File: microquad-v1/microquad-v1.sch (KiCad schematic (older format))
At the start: 22 parts

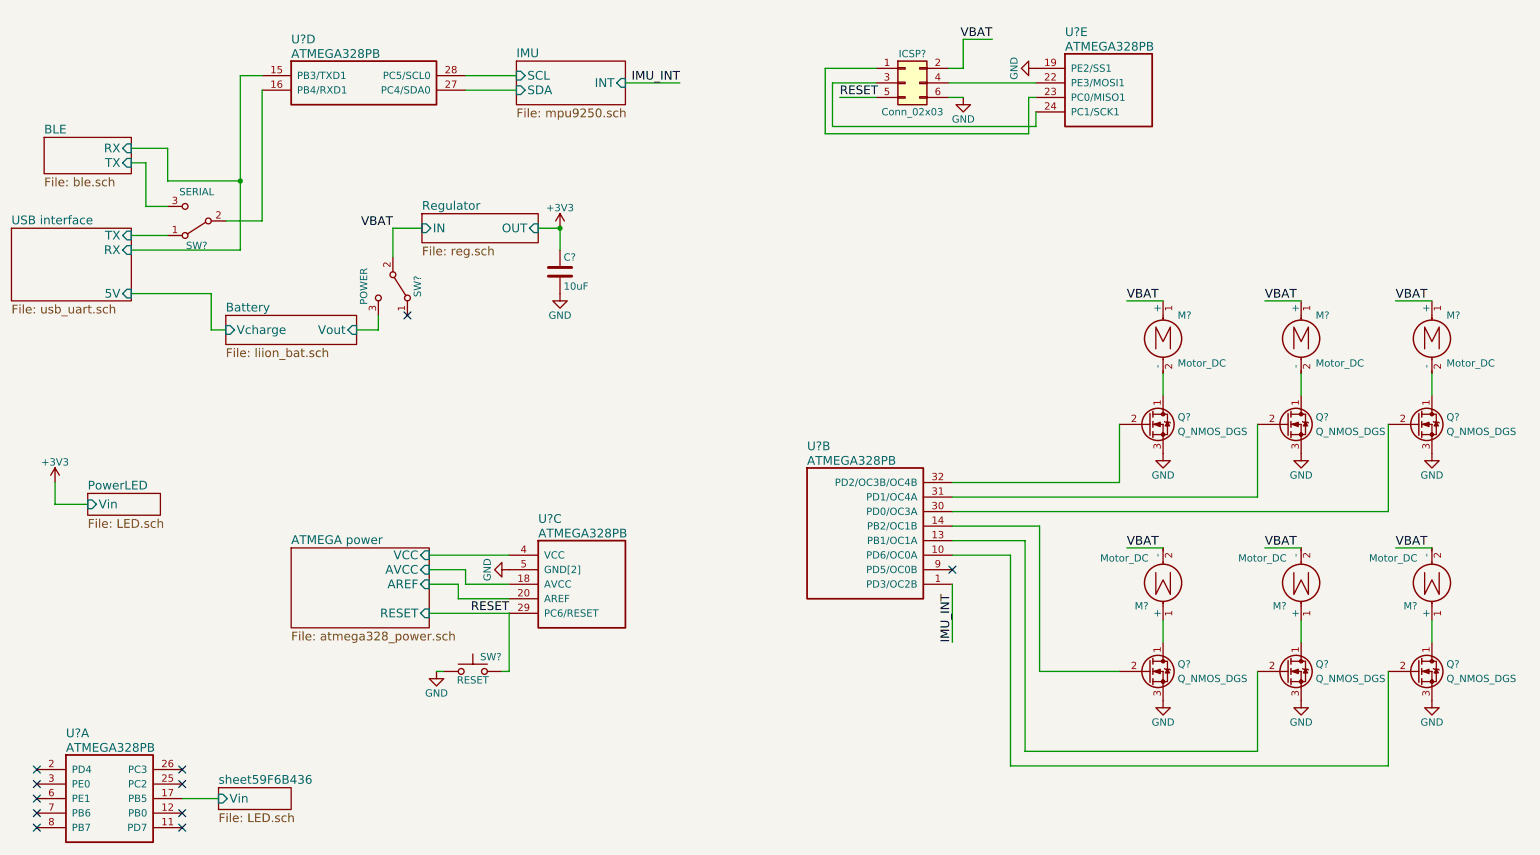
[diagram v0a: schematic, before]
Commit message: Fixed DRC errors (the ladybug is now happy)
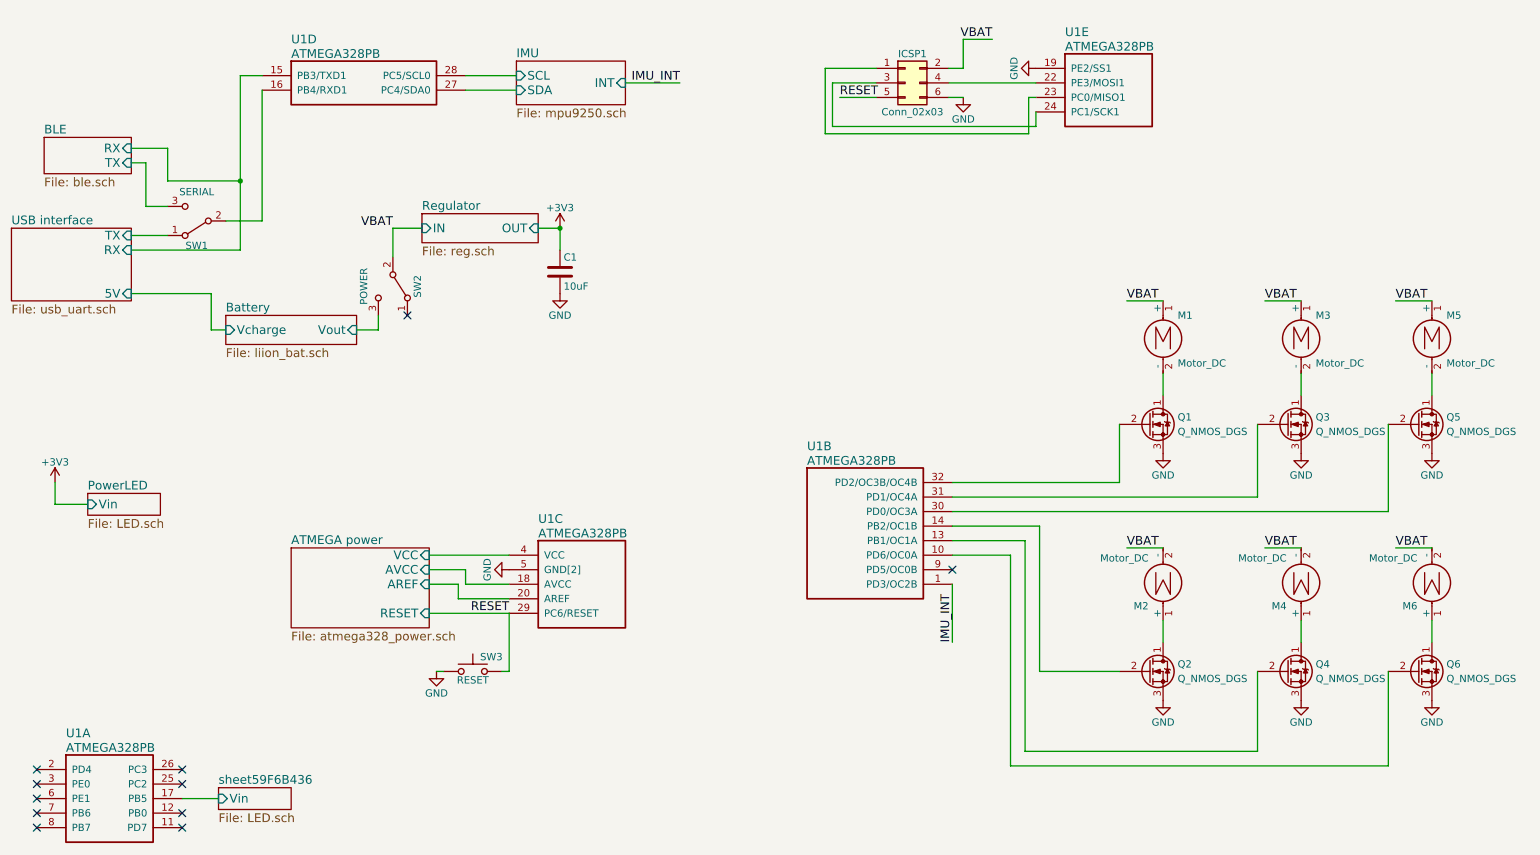
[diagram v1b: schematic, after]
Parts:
- gave numbers to parts that had none: 18
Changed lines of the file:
@@
 $Descr A4 11693 8268
 encoding utf-8
-Sheet 1 8
+Sheet 1 9
 Title ""
 Date ""
@@
 $EndSheet
 $Comp
-L ATMEGA328PB U?
+L ATMEGA328PB U1
 U 2 1 59F26F3B
 P 6000 4050
-F 0 "U?" H 6200 4300 60  0000 L CNN
+F 0 "U1" H 6200 4300 60  0000 L CNN
 F 1 "ATMEGA328PB" H 6200 4200 60  0000 L CNN
 F 2 "" H 6000 4050 60  0001 C CNN
@@
 $EndComp
 $Comp
-L ATMEGA328PB U?
+L ATMEGA328PB U1
 U 1 1 59F2742E
 P 900 6025
-F 0 "U?" H 1100 6275 60  0000 L CNN
+F 0 "U1" H 1100 6275 60  0000 L CNN
 F 1 "ATMEGA328PB" H 1100 6175 60  0000 L CNN
 F 2 "" H 900 6025 60  0001 C CNN
@@
 $EndComp
 $Comp
-L ATMEGA328PB U?
+L ATMEGA328PB U1
 U 3 1 59F274A5
 P 4150 4550
-F 0 "U?" H 4350 4800 60  0000 L CNN
+F 0 "U1" H 4350 4800 60  0000 L CNN
 F 1 "ATMEGA328PB" H 4350 4700 60  0000 L CNN
 F 2 "" H 4150 4550 60  0001 C CNN
@@
 $EndComp
 $Comp
-L ATMEGA328PB U?
+L ATMEGA328PB U1
 U 4 1 59F27516
 P 2450 1250
-F 0 "U?" H 2650 1500 60  0000 L CNN
+F 0 "U1" H 2650 1500 60  0000 L CNN
 F 1 "ATMEGA328PB" H 2650 1400 60  0000 L CNN
 F 2 "" H 2450 1250 60  0001 C CNN
@@
 $EndComp
 $Comp
-L ATMEGA328PB U?
+L ATMEGA328PB U1
 U 5 1 59F275A9
 P 7775 1200
-F 0 "U?" H 7975 1450 60  0000 L CNN
+F 0 "U1" H 7975 1450 60  0000 L CNN
 F 1 "ATMEGA328PB" H 7975 1350 60  0000 L CNN
 F 2 "" H 7775 1200 60  0001 C CNN
@@
 $EndComp
 $Comp
-L C C?
+L C C1
 U 1 1 59F54C39
 P 4500 2600
-F 0 "C?" H 4525 2700 50  0000 L CNN
+F 0 "C1" H 4525 2700 50  0000 L CNN
 F 1 "10uF" H 4525 2500 50  0000 L CNN
 F 2 "Capacitors_SMD:C_0805" H 4538 2450 50  0001 C CNN
@@
 NoConn ~ 3450 2900
 $Comp
-L Q_NMOS_DGS Q?
+L Q_NMOS_DGS Q1
 U 1 1 59F6C2EB
 P 8550 3650
-F 0 "Q?" H 8750 3700 50  0000 L CNN
+F 0 "Q1" H 8750 3700 50  0000 L CNN
 F 1 "Q_NMOS_DGS" H 8750 3600 50  0000 L CNN
 F 2 "" H 8750 3750 50  0001 C CNN
@@
 $EndComp
 $Comp
-L GND #PWR?
+L GND #PWR04
 U 1 1 59F6C628
 P 8650 3850
-F 0 "#PWR?" H 8650 3600 50  0001 C CNN
+F 0 "#PWR04" H 8650 3600 50  0001 C CNN
 F 1 "GND" H 8650 3700 50  0000 C CNN
 F 2 "" H 8650 3850 50  0001 C CNN
@@
 VBAT
 $Comp
-L Motor_DC M?
+L Motor_DC M1
 U 1 1 59F6E11F
 P 8650 3000
-F 0 "M?" H 8750 3100 50  0000 L CNN
+F 0 "M1" H 8750 3100 50  0000 L CNN
 F 1 "Motor_DC" H 8750 2800 50  0000 L TNN
 F 2 "" H 8650 2910 50  0001 C CNN
@@
 	8650 3300 8650 3450
 $Comp
-L Q_NMOS_DGS Q?
+L Q_NMOS_DGS Q3
 U 1 1 59F6F67A
 P 9500 3650
-F 0 "Q?" H 9700 3700 50  0000 L CNN
+F 0 "Q3" H 9700 3700 50  0000 L CNN
 F 1 "Q_NMOS_DGS" H 9700 3600 50  0000 L CNN
 F 2 "" H 9700 3750 50  0001 C CNN
@@
 $EndComp
 $Comp
-L GND #PWR?
+L GND #PWR05
 U 1 1 59F6F680
 P 9600 3850
-F 0 "#PWR?" H 9600 3600 50  0001 C CNN
+F 0 "#PWR05" H 9600 3600 50  0001 C CNN
 F 1 "GND" H 9600 3700 50  0000 C CNN
 F 2 "" H 9600 3850 50  0001 C CNN
@@
 VBAT
 $Comp
-L Motor_DC M?
+L Motor_DC M3
 U 1 1 59F6F688
 P 9600 3000
-F 0 "M?" H 9700 3100 50  0000 L CNN
+F 0 "M3" H 9700 3100 50  0000 L CNN
 F 1 "Motor_DC" H 9700 2800 50  0000 L TNN
 F 2 "" H 9600 2910 50  0001 C CNN
@@
 	9600 3300 9600 3450
 $Comp
-L Q_NMOS_DGS Q?
+L Q_NMOS_DGS Q5
 U 1 1 59F6F948
 P 10400 3650
-F 0 "Q?" H 10600 3700 50  0000 L CNN
+F 0 "Q5" H 10600 3700 50  0000 L CNN
 F 1 "Q_NMOS_DGS" H 10600 3600 50  0000 L CNN
 F 2 "" H 10600 3750 50  0001 C CNN
@@
 $EndComp
 $Comp
-L GND #PWR?
+L GND #PWR06
 U 1 1 59F6F94E
 P 10500 3850
-F 0 "#PWR?" H 10500 3600 50  0001 C CNN
+F 0 "#PWR06" H 10500 3600 50  0001 C CNN
 F 1 "GND" H 10500 3700 50  0000 C CNN
 F 2 "" H 10500 3850 50  0001 C CNN
@@
 VBAT
 $Comp
-L Motor_DC M?
+L Motor_DC M5
 U 1 1 59F6F955
 P 10500 3000
-F 0 "M?" H 10600 3100 50  0000 L CNN
+F 0 "M5" H 10600 3100 50  0000 L CNN
 F 1 "Motor_DC" H 10600 2800 50  0000 L TNN
 F 2 "" H 10500 2910 50  0001 C CNN
@@
 	10200 3650 10200 4250
 $Comp
-L Q_NMOS_DGS Q?
+L Q_NMOS_DGS Q2
 U 1 1 59F700F6
 P 8550 5350
-F 0 "Q?" H 8750 5400 50  0000 L CNN
+F 0 "Q2" H 8750 5400 50  0000 L CNN
 F 1 "Q_NMOS_DGS" H 8750 5300 50  0000 L CNN
 F 2 "" H 8750 5450 50  0001 C CNN
@@
 $EndComp
 $Comp
-L GND #PWR?
+L GND #PWR07
 U 1 1 59F700FC
 P 8650 5550
-F 0 "#PWR?" H 8650 5300 50  0001 C CNN
+F 0 "#PWR07" H 8650 5300 50  0001 C CNN
 F 1 "GND" H 8650 5400 50  0000 C CNN
 F 2 "" H 8650 5550 50  0001 C CNN
@@
 VBAT
 $Comp
-L Motor_DC M?
+L Motor_DC M2
 U 1 1 59F70103
 P 8650 4800
-F 0 "M?" H 8750 4900 50  0000 L CNN
+F 0 "M2" H 8750 4900 50  0000 L CNN
 F 1 "Motor_DC" H 8750 4600 50  0000 L TNN
 F 2 "" H 8650 4710 50  0001 C CNN
@@
 	8650 5000 8650 5150
 $Comp
-L Q_NMOS_DGS Q?
+L Q_NMOS_DGS Q4
 U 1 1 59F7010B
 P 9500 5350
-F 0 "Q?" H 9700 5400 50  0000 L CNN
+F 0 "Q4" H 9700 5400 50  0000 L CNN
 F 1 "Q_NMOS_DGS" H 9700 5300 50  0000 L CNN
 F 2 "" H 9700 5450 50  0001 C CNN
@@
 $EndComp
 $Comp
-L GND #PWR?
+L GND #PWR08
 U 1 1 59F70111
 P 9600 5550
-F 0 "#PWR?" H 9600 5300 50  0001 C CNN
+F 0 "#PWR08" H 9600 5300 50  0001 C CNN
 F 1 "GND" H 9600 5400 50  0000 C CNN
 F 2 "" H 9600 5550 50  0001 C CNN
@@
 VBAT
 $Comp
-L Motor_DC M?
+L Motor_DC M4
 U 1 1 59F70118
 P 9600 4800
-F 0 "M?" H 9700 4900 50  0000 L CNN
+F 0 "M4" H 9700 4900 50  0000 L CNN
 F 1 "Motor_DC" H 9700 4600 50  0000 L TNN
 F 2 "" H 9600 4710 50  0001 C CNN
@@
 	9300 5350 9300 5900
 $Comp
-L Q_NMOS_DGS Q?
+L Q_NMOS_DGS Q6
 U 1 1 59F70122
 P 10400 5350
-F 0 "Q?" H 10600 5400 50  0000 L CNN
+F 0 "Q6" H 10600 5400 50  0000 L CNN
 F 1 "Q_NMOS_DGS" H 10600 5300 50  0000 L CNN
 F 2 "" H 10600 5450 50  0001 C CNN
@@
 $EndComp
 $Comp
-L GND #PWR?
+L GND #PWR09
 U 1 1 59F70128
 P 10500 5550
-F 0 "#PWR?" H 10500 5300 50  0001 C CNN
+F 0 "#PWR09" H 10500 5300 50  0001 C CNN
 F 1 "GND" H 10500 5400 50  0000 C CNN
 F 2 "" H 10500 5550 50  0001 C CNN
@@
 VBAT
 $Comp
-L Motor_DC M?
+L Motor_DC M6
 U 1 1 59F7012F
 P 10500 4800
-F 0 "M?" H 10600 4900 50  0000 L CNN
+F 0 "M6" H 10600 4900 50  0000 L CNN
 F 1 "Motor_DC" H 10600 4600 50  0000 L TNN
 F 2 "" H 10500 4710 50  0001 C CNN
@@
 $EndSheet
 $Comp
-L +3V3 #PWR?
+L +3V3 #PWR010
 U 1 1 59F6B9F3
 P 1025 4050
-F 0 "#PWR?" H 1025 3900 50  0001 C CNN
+F 0 "#PWR010" H 1025 3900 50  0001 C CNN
 F 1 "+3V3" H 1025 4190 50  0000 C CNN
 F 2 "" H 1025 4050 50  0001 C CNN
@@
 	1900 6225 2150 6225
 $Comp
-L SW_Push SW?
+L SW_Push SW3
 U 1 1 59F7EEE0
 P 3900 5350
-F 0 "SW?" H 3950 5450 50  0000 L CNN
+F 0 "SW3" H 3950 5450 50  0000 L CNN
 F 1 "RESET" H 3900 5290 50  0000 C CNN
 F 2 "" H 3900 5550 50  0001 C CNN
@@
 $EndComp
 $Comp
-L GND #PWR?
+L GND #PWR011
 U 1 1 59F7EFD3
 P 3650 5350
-F 0 "#PWR?" H 3650 5100 50  0001 C CNN
+F 0 "#PWR011" H 3650 5100 50  0001 C CNN
 F 1 "GND" H 3650 5200 50  0000 C CNN
 F 2 "" H 3650 5350 50  0001 C CNN
@@
 	4150 5350 4100 5350
 $Comp
-L Conn_02x03_Odd_Even ICSP?
+L Conn_02x03_Odd_Even ICSP1
 U 1 1 59F84B16
 P 6875 1300
-F 0 "ICSP?" H 6925 1500 50  0000 C CNN
+F 0 "ICSP1" H 6925 1500 50  0000 C CNN
 F 1 "Conn_02x03" H 6925 1100 50  0000 C CNN
 F 2 "" H 6875 1300 50  0001 C CNN
@@
 	7175 1400 7275 1400
 $Comp
-L GND #PWR?
+L GND #PWR012
 U 1 1 59F8679D
 P 7275 1400
-F 0 "#PWR?" H 7275 1150 50  0001 C CNN
+F 0 "#PWR012" H 7275 1150 50  0001 C CNN
 F 1 "GND" H 7275 1250 50  0000 C CNN
 F 2 "" H 7275 1400 50  0001 C CNN
@@
 RESET
 $Comp
-L GND #PWR?
+L GND #PWR013
 U 1 1 59F8B068
 P 7775 1200
-F 0 "#PWR?" H 7775 950 50  0001 C CNN
+F 0 "#PWR013" H 7775 950 50  0001 C CNN
 F 1 "GND" H 7775 1050 50  0000 C CNN
 F 2 "" H 7775 1200 50  0001 C CNN
@@
 	7200 4750 7200 5150
 $Comp
-L SW_SPDT SW?
+L SW_SPDT SW2
 U 1 1 59F9E6E3
 P 3350 2700
-F 0 "SW?" H 3350 2870 50  0000 C CNN
+F 0 "SW2" H 3350 2870 50  0000 C CNN
 F 1 "POWER" H 3350 2500 50  0000 C CNN
 F 2 "" H 3350 2700 50  0001 C CNN
@@
 $EndComp
 $Comp
-L SW_SPDT SW?
+L SW_SPDT SW1
 U 1 1 59F9E9A3
 P 2000 2250
-F 0 "SW?" H 2000 2420 50  0000 C CNN
+F 0 "SW1" H 2000 2420 50  0000 C CNN
 F 1 "SERIAL" H 2000 2050 50  0000 C CNN
 F 2 "" H 2000 2250 50  0001 C CNN

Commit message: Notes from schematic review
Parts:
- added D?: D, symbol D
- added D?: D_Zener, symbol D_Zener
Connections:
- net +3V3: now also ICSP1.2 (Pin_2)
- net VBAT: no longer ICSP1.2 (Pin_2)
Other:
- note added: "DPDT switch?\n"
- note added: "Diodes?"
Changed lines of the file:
@@
 P 8550 3650
 F 0 "Q1" H 8750 3700 50  0000 L CNN
-F 1 "Q_NMOS_DGS" H 8750 3600 50  0000 L CNN
+F 1 "Q_NMOS_DGS" H 8400 3500 50  0000 L CNN
 F 2 "" H 8750 3750 50  0001 C CNN
 F 3 "" H 8550 3650 50  0001 C CNN
@@
 	7275 1200 7275 1000
 Wire Wire Line
-	7275 1000 7475 1000
-Text Label 7475 1000 2    60   ~ 0
-VBAT
-Wire Wire Line
 	7175 1400 7275 1400
 $Comp
@@
 Wire Wire Line
 	5325 1300 4950 1300
+Text Notes 7650 3100 0    60   ~ 0
+Diodes?
+$Comp
+L D D?
+U 1 1 59F7DE54
+P 8325 3075
+F 0 "D?" H 8325 3175 50  0000 C CNN
+F 1 "D" H 8325 2975 50  0000 C CNN
+F 2 "" H 8325 3075 50  0001 C CNN
+F 3 "" H 8325 3075 50  0001 C CNN
+	1    8325 3075
+	0    1    1    0
+$EndComp
+Text Notes 2475 2025 0    60   ~ 0
+DPDT switch?\n
+$Comp
+L +3V3 #PWR?
+U 1 1 59F86353
+P 7275 1000
+F 0 "#PWR?" H 7275 850 50  0001 C CNN
+F 1 "+3V3" H 7275 1140 50  0000 C CNN
+F 2 "" H 7275 1000 50  0001 C CNN
+F 3 "" H 7275 1000 50  0001 C CNN
+	1    7275 1000
+	1    0    0    -1
+$EndComp
+$Comp
+L D_Zener D?
+U 1 1 59F87D4C
+P 9050 3675
+F 0 "D?" H 9050 3775 50  0000 C CNN
+F 1 "D_Zener" H 9050 3575 50  0000 C CNN
+F 2 "" H 9050 3675 50  0001 C CNN
+F 3 "" H 9050 3675 50  0001 C CNN
+	1    9050 3675
+	0    1    1    0
+$EndComp
 $EndSCHEMATC
